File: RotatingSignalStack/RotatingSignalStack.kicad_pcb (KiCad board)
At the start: 2 copper layers, 64.1 x 54 mm, 96 parts, among them IC2 STM32H562RIT6, J1 Conn_01x06, J2 Conn_01x04, J3 RJ45_LED_Shielded, J4 Conn_01x09, SW1 SW_Push, SW5 SW_Push, SW6 SW_Push, SW7 SW_Push, T1 GMG116S1202R, U1 TMAG5273C1QDBVR, U2 AP63203WU-7, U3 SN65HVD232, U4 DP83825I, U5 SG-210STF 50.0000ML0, U6 USBLC6-2SC6, U7 USBLC6-4SC6, U8 OKI-78SR-3.3_1.5-W36-C

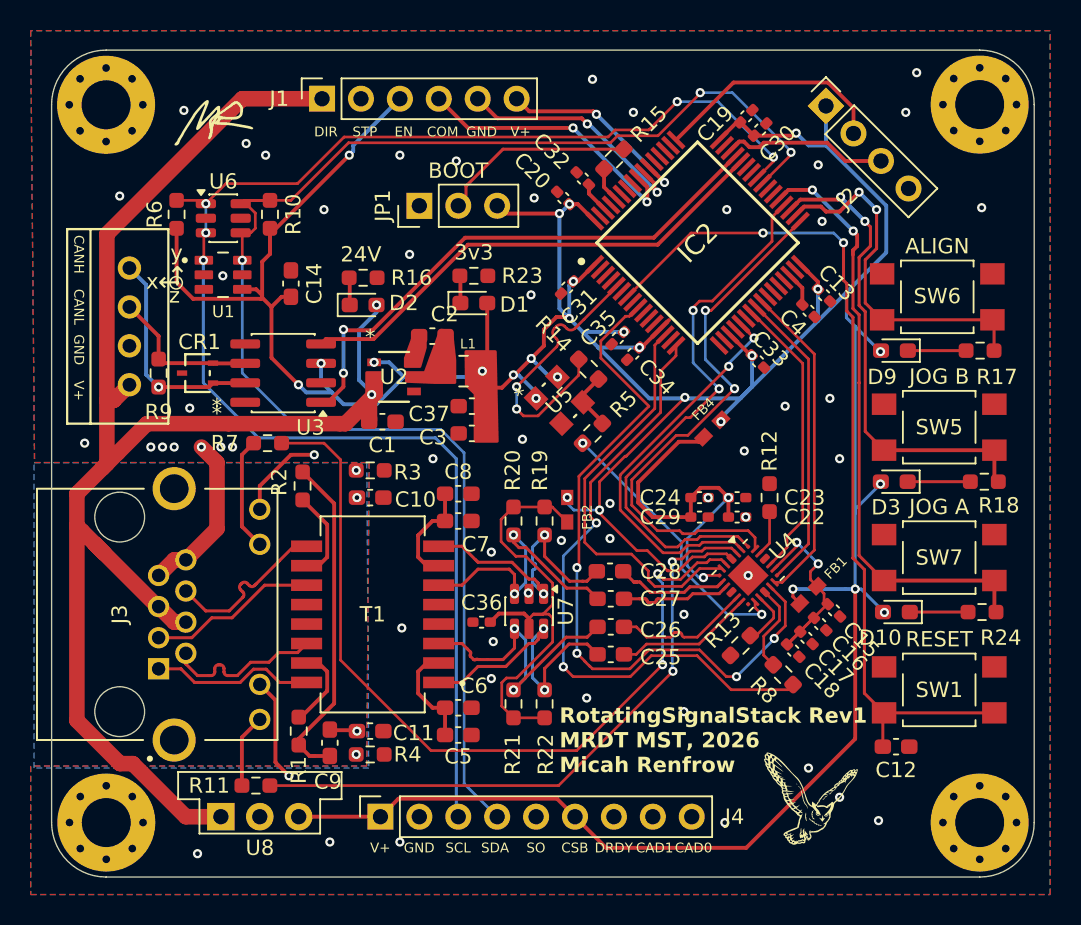
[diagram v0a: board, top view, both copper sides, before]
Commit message: fix incorrect pin labels
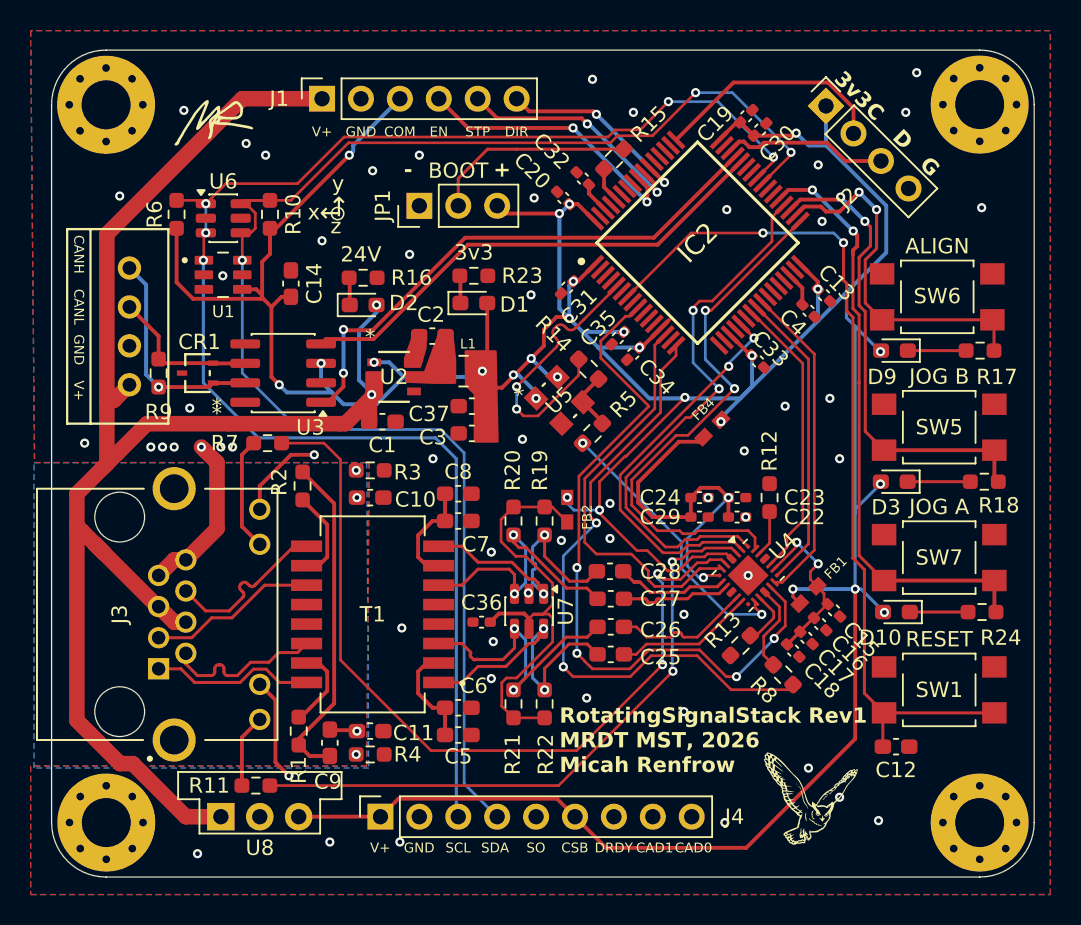
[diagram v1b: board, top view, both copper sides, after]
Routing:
- net Net-(JP1-C): track 11.9 -> 13.4 mm
- net +3V3: track 265.9 -> 266.6 mm
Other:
- board text added: "+"
- board text added: "-"
- board text added: "C"
- board text added: "D"
- board text added: "G"

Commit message: Final design as ordered
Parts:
- moved R9 2.65 mm to (134.9, 77.0), turned to 180 degrees
- moved CR1 1.80 mm to (135.1, 74.4), turned to 90 degrees
- moved U8 1.02 mm to (136.4, 106.2)
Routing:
- net /CAN/CANL: track 10.1 -> 13.1 mm, vias 0 -> 2
- net /CAN/CANH: track 14.3 -> 13.1 mm, vias 1 -> 0
- net GND: vias 56 -> 197
